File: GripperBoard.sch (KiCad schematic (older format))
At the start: 21 parts, among them J1 UART, J10 MOT2_AOUT2, J11 MOT2_BOUT1, J12 MOT2_BOUT2, J2 CAN_1, J3 CAN_2, J4 SWD, J5 MOT1_AOUT1, J6 MOT1_AOUT2, J7 MOT1_BOUT1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

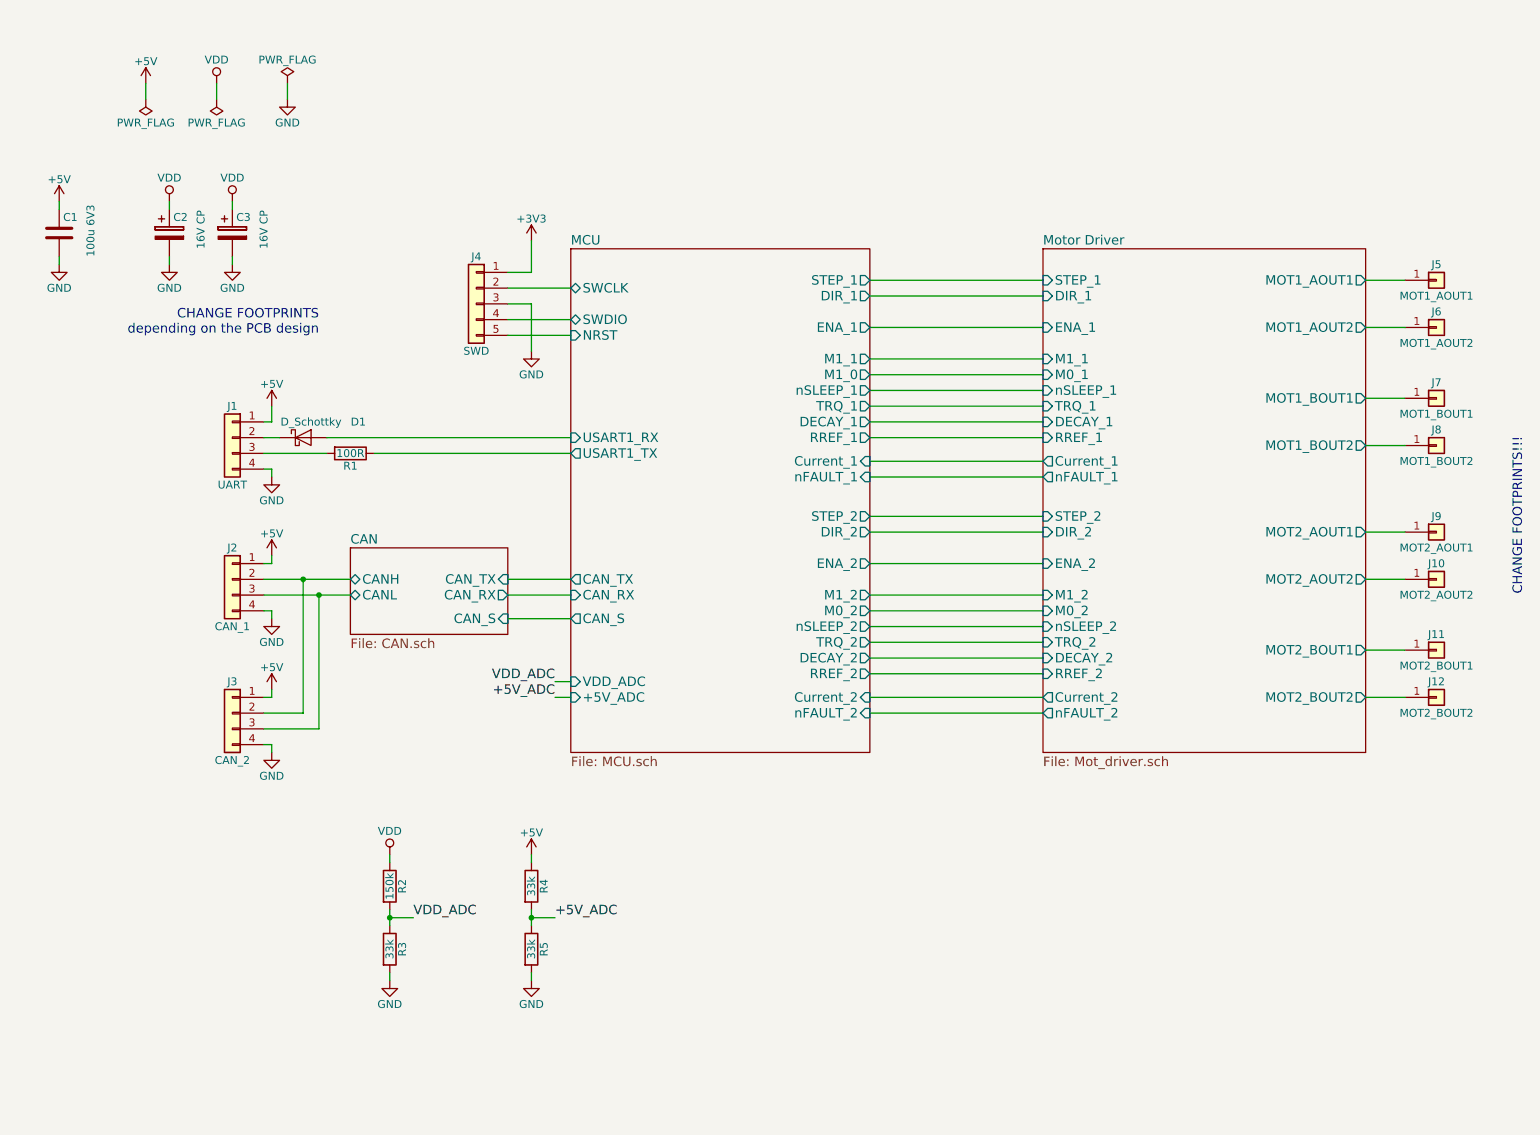
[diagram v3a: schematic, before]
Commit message: started modifying for 3 stepper motors
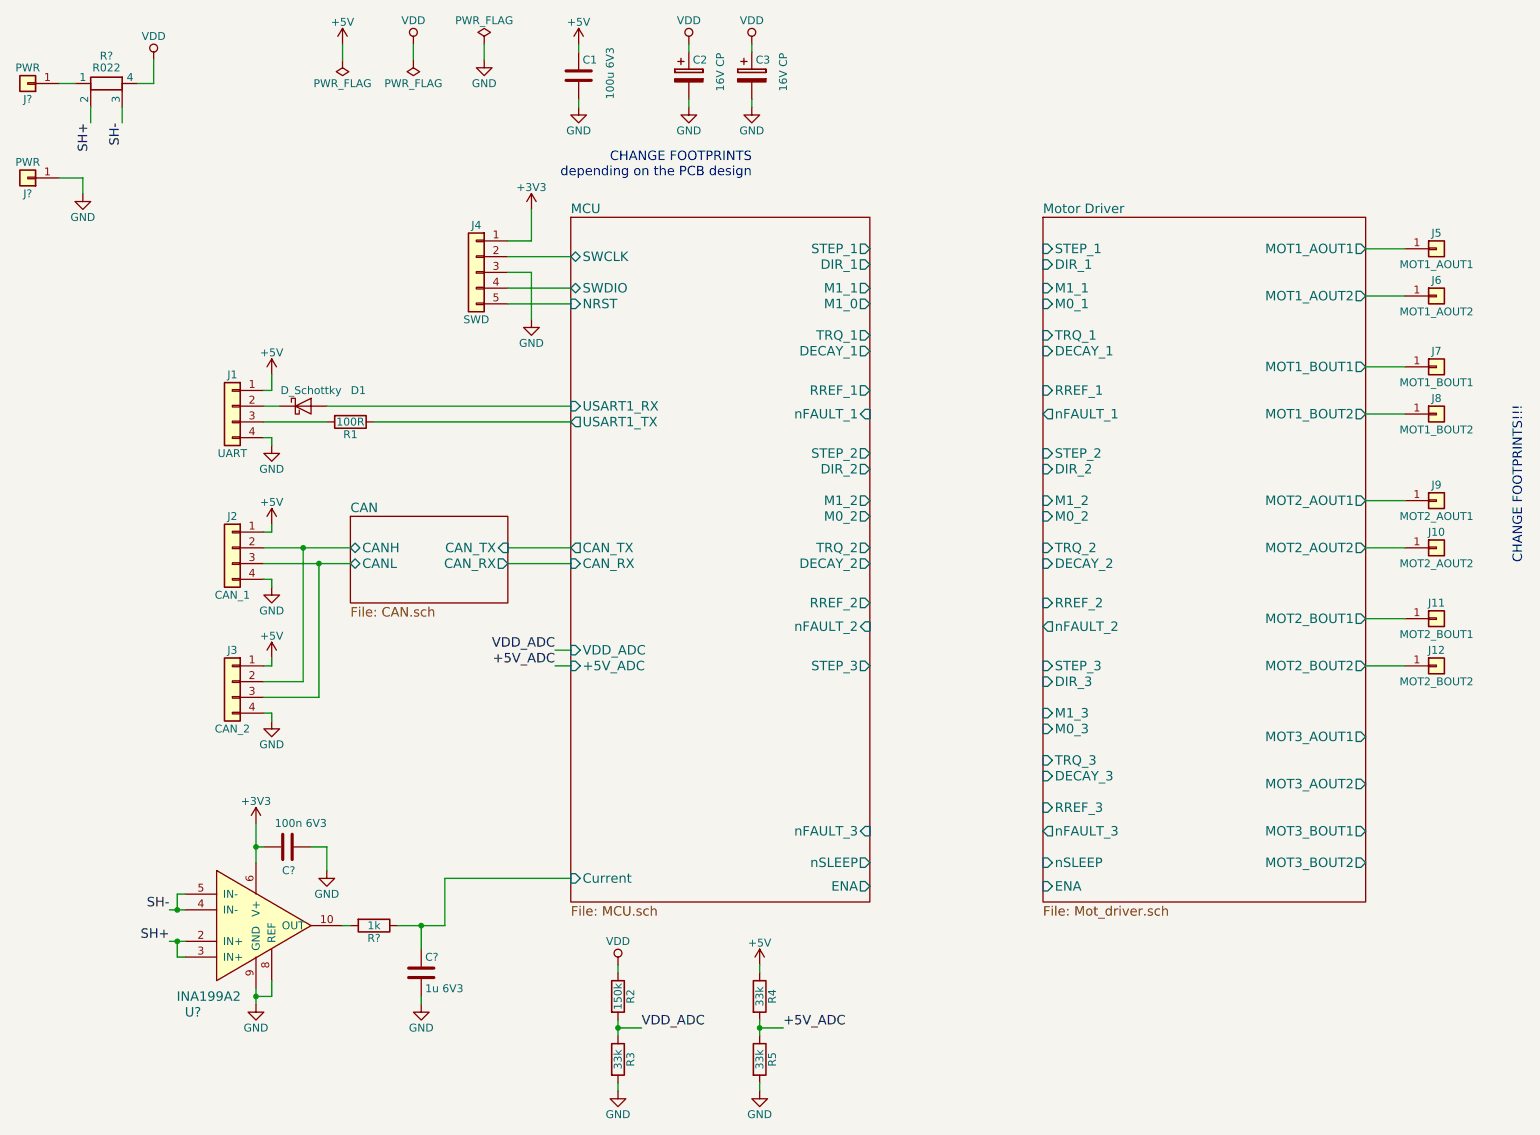
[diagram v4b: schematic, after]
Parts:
- added C?: 100n 6V3, Capacitors_SMD:C_0402, symbol C
- added C?: 1u 6V3, Capacitors_SMD:C_0402, symbol C
- added J? (x2): PWR, symbol Conn_01x01
- added R?: R022, lakotamm-shunt:R_0603, symbol R_Shunt
- added R?: 1k, Resistors_SMD:R_0402, symbol R
- added U?: INA199A2, Housings_DFN_QFN:UQFN-10_1.4x1.8mm_Pitch0.4mm, symbol INA199
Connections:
- net +3V3: now also C?.1, U?.6 (V+)
- net GND: now also C?.2, C?.2, J?.1 (Pin_1), U?.8 (REF), U?.9 (GND)
- net VDD: now also R?.4
- new net: J?.1 (Pin_1), R?.1
- new net: R?.2, U?.10 (OUT)
- new net MCU/Current: C?.1, R?.1
- new net SH+: R?.2, U?.2 (IN+), U?.3 (IN+)
- new net SH-: R?.3, U?.4 (IN-), U?.5 (IN-)
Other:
- moved on the sheet: C1, C2, C3, D1, J1, J10, J11, J12, J2, J3, J4, J5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
